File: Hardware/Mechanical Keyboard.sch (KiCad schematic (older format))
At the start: 24 parts, among them J1 USBMINI_B05, U1 ATMEGA32U4-AU, U2 IS31FL3731-SALS2, X1 ASX4

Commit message: Move diodes and resistors
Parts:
- C1, C2, C3, C4, C5, C6: symbol C -> Device:C
- J1: symbol USBMINI_B05 -> oupiin_usb:USBMINI_B05
- R1, R10, R11, R12, R13, R2, R3, R4, R5, R6, R7, R8, R9: symbol R -> Device:R
- S101: symbol DTSM-6 -> dtsjw:DTSM-6
- U1: symbol ATMEGA32U4-AU -> Mechanical-Keyboard-rescue:ATMEGA32U4-AU
- U2: symbol IS31FL3731-SALS2 -> ai03-locallib:IS31FL3731-SALS2
- X1: symbol ASX4 -> aker:ASX4
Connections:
- wire segments 143 -> 157

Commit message: refactor
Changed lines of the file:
@@
 Text Label 5800 5400 0    60   ~ 0
 swm_col3
-Text Label 5800 4700 0    60   ~ 0
+Text Label 5800 6600 0    60   ~ 0
 swm_col4
 Text Label 5800 5300 0    60   ~ 0
 swm_col5
-Text Label 5800 6600 0    60   ~ 0
+Text Label 5800 4700 0    60   ~ 0
 swm_col9
 Text Label 5800 6500 0    60   ~ 0
@@
 Wire Wire Line
 	13150 4000 12800 4000
+Text Label 13150 4100 2    60   ~ 0
+led_ca1
+Text Label 14250 4500 2    60   ~ 0
+led_ca2
+Text Label 13150 4300 2    60   ~ 0
+led_ca3
+Text Label 13150 3900 2    60   ~ 0
+led_ca4
+Text Label 13150 4000 2    60   ~ 0
+led_ca5
+Text Label 13150 4400 2    60   ~ 0
+led_ca6
+Text Label 13150 4500 2    60   ~ 0
+led_ca7
 Text Label 13150 3800 2    60   ~ 0
-led_ca1
-Text Label 13150 3900 2    60   ~ 0
-led_ca2
-Text Label 13150 4000 2    60   ~ 0
-led_ca3
-Text Label 13150 4100 2    60   ~ 0
-led_ca4
+led_ca8
 Text Label 13150 4200 2    60   ~ 0
-led_ca5
-Text Label 13150 4300 2    60   ~ 0
-led_ca6
-Text Label 13150 4400 2    60   ~ 0
-led_ca7
-Text Label 13150 4500 2    60   ~ 0
-led_ca8
-Text Label 14250 4500 2    60   ~ 0
 led_ca9
 Wire Wire Line

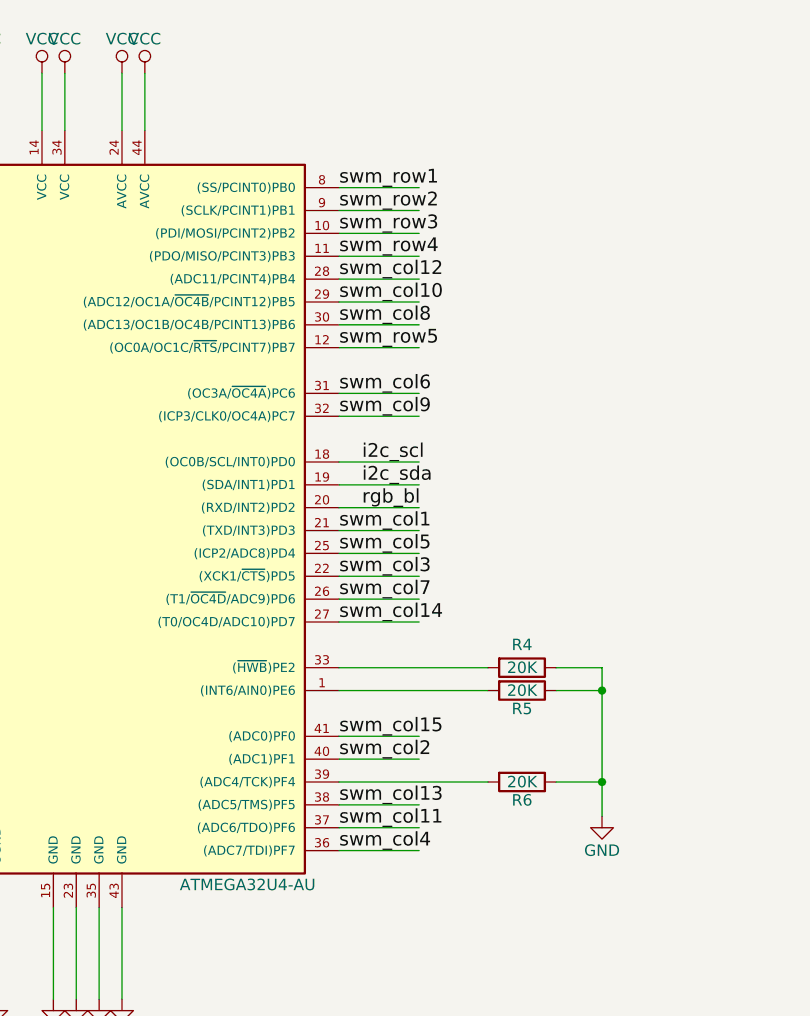
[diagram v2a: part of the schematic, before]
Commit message: Keyboard tracking was finished. Only GND circuit is left
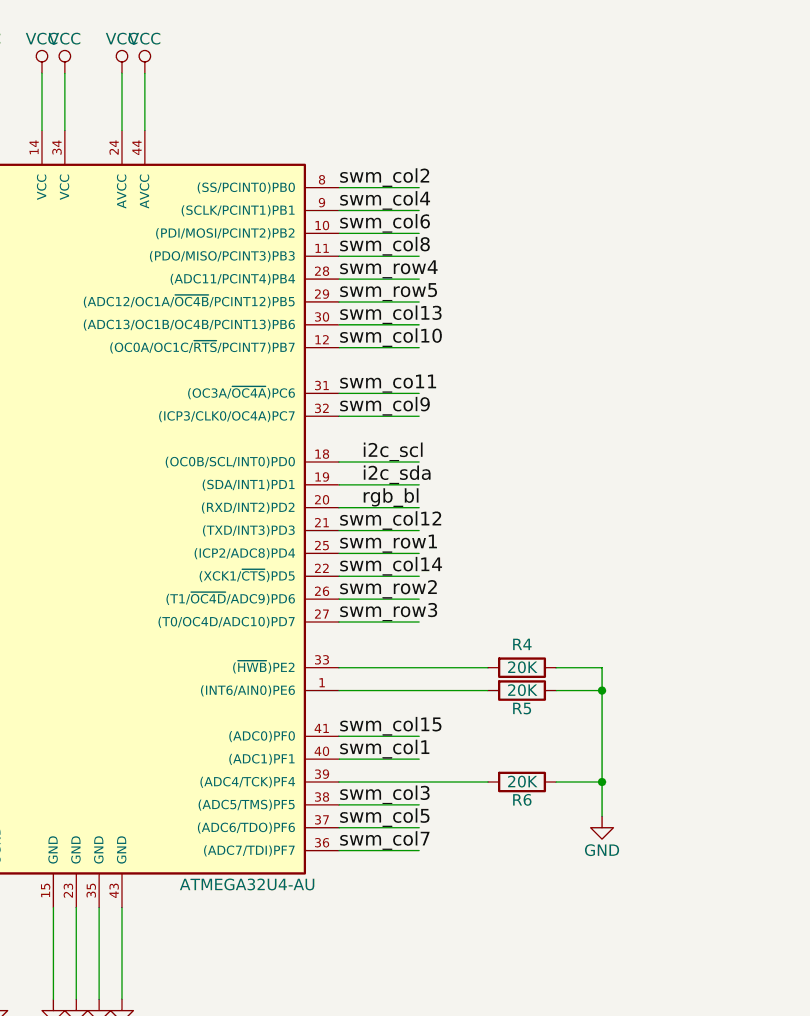
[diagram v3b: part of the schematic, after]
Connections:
- net labels added: swm_co11
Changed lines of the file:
@@
 swm_col14
 Text Label 5800 5200 0    60   ~ 0
+swm_col12
+Text Label 5800 6200 0    60   ~ 0
 swm_col1
-Text Label 5800 6200 0    60   ~ 0
-swm_col2
 Text Label 5800 5400 0    60   ~ 0
-swm_col3
+swm_col14
 Text Label 5800 6600 0    60   ~ 0
-swm_col4
+swm_col7
 Text Label 5800 5300 0    60   ~ 0
-swm_col5
+swm_row1
 Text Label 5800 4700 0    60   ~ 0
 swm_col9
 Text Label 5800 6500 0    60   ~ 0
-swm_col11
+swm_col5
 Text Label 5800 6400 0    60   ~ 0
-swm_col13
+swm_col3
 Text Label 5800 6100 0    60   ~ 0
 swm_col15
 Text Label 5800 5600 0    60   ~ 0
-swm_col14
+swm_row3
 Text Label 5800 5500 0    60   ~ 0
-swm_col7
+swm_row2
 Text Label 5800 4600 0    60   ~ 0
-swm_col6
+swm_co11
 Text Label 5800 4300 0    60   ~ 0
-swm_col8
+swm_col13
 Text Label 5800 4200 0    60   ~ 0
-swm_col10
+swm_row5
 Text Label 5800 4100 0    60   ~ 0
-swm_col12
+swm_row4
 Text Label 8500 3600 2    60   ~ 0
 swm_row1
@@
 swm_row5
 Text Label 5800 3700 0    60   ~ 0
-swm_row1
+swm_col2
 Text Label 5800 3800 0    60   ~ 0
-swm_row2
+swm_col4
 Text Label 5800 3900 0    60   ~ 0
-swm_row3
+swm_col6
 Text Label 5800 4000 0    60   ~ 0
-swm_row4
+swm_col8
 Text Label 5800 4400 0    60   ~ 0
-swm_row5
+swm_col10
 Text Label 11200 5900 2    60   ~ 0
 rgb_bl

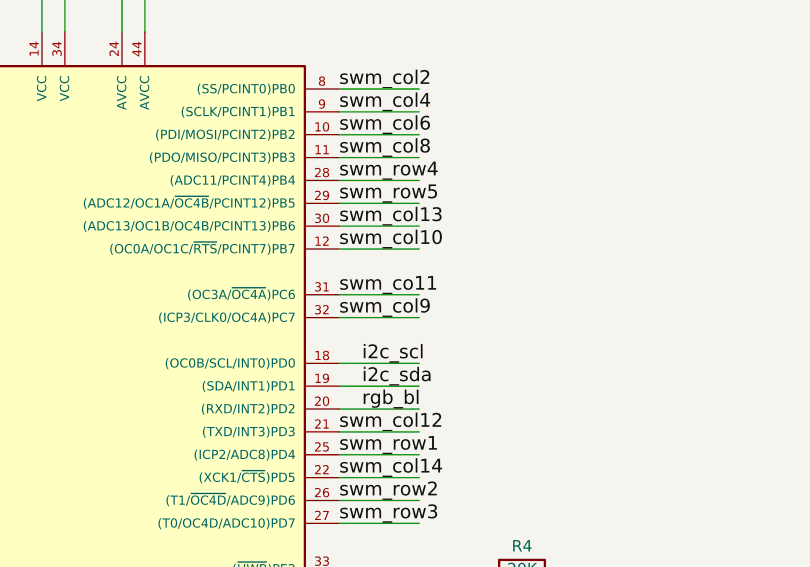
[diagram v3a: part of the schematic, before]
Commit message: Bugfix for swm_col9
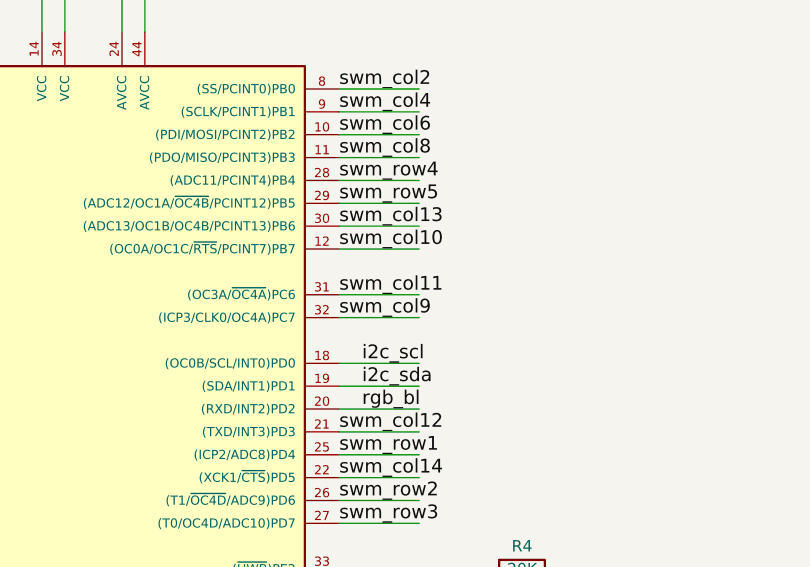
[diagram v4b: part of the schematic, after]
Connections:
- net labels removed: swm_co11
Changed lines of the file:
@@
 swm_row2
 Text Label 5800 4600 0    60   ~ 0
-swm_co11
+swm_col11
 Text Label 5800 4300 0    60   ~ 0
 swm_col13

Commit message: add driling holes
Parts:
- C1, C2, C3, C4, C5, C6: symbol Device:C -> Mechanical-Keyboard-rescue:C-Device
- R1, R10, R11, R12, R13, R2, R3, R4, R5, R6, R7, R8, R9: symbol Device:R -> Mechanical-Keyboard-rescue:R-Device
- U1: symbol Mechanical-Keyboard-rescue:ATMEGA32U4-AU -> Mechanical-Keyboard-rescue:ATMEGA32U4-AU-Mechanical-Keyboard-rescue
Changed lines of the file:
@@
 $EndSheet
 $Comp
-L power:GND #PWR01
+L Mechanical-Keyboard-rescue:GND-power #PWR01
 U 1 1 5C542506
 P 4750 7250
@@
 $EndComp
 $Comp
-L Mechanical-Keyboard-rescue:ATMEGA32U4-AU U1
+L Mechanical-Keyboard-rescue:ATMEGA32U4-AU-Mechanical-Keyboard-rescue U1
 U 1 1 5C4F1518
 P 4700 5250
@@
 $EndSheet
 $Comp
-L Device:R R7
+L Mechanical-Keyboard-rescue:R-Device R7
 U 1 1 5C4FF9D5
 P 11350 5900
@@
 $EndComp
 $Comp
-L power:VCC #PWR02
+L Mechanical-Keyboard-rescue:VCC-power #PWR02
 U 1 1 5C5072B7
 P 4500 3200
@@
 $EndComp
 $Comp
-L power:VCC #PWR03
+L Mechanical-Keyboard-rescue:VCC-power #PWR03
 U 1 1 5C50759B
 P 14650 3900
@@
 $EndComp
 $Comp
-L power:GND #PWR04
+L Mechanical-Keyboard-rescue:GND-power #PWR04
 U 1 1 5C507696
 P 14950 4250
@@
 $EndComp
 $Comp
-L power:VCC #PWR05
+L Mechanical-Keyboard-rescue:VCC-power #PWR05
 U 1 1 5C5087DF
 P 11100 6050
@@
 $EndComp
 $Comp
-L power:GND #PWR06
+L Mechanical-Keyboard-rescue:GND-power #PWR06
 U 1 1 5C508883
 P 11100 6200
@@
 $EndComp
 $Comp
-L power:GND #PWR07
+L Mechanical-Keyboard-rescue:GND-power #PWR07
 U 1 1 5C50B929
 P 11800 3550
@@
 $EndComp
 $Comp
-L power:GND #PWR08
+L Mechanical-Keyboard-rescue:GND-power #PWR08
 U 1 1 5C50C0CD
 P 6950 6450
@@
 $EndComp
 $Comp
-L Device:R R2
+L Mechanical-Keyboard-rescue:R-Device R2
 U 1 1 5C50D36F
 P 3150 5050
@@
 $EndComp
 $Comp
-L Device:R R3
+L Mechanical-Keyboard-rescue:R-Device R3
 U 1 1 5C50D676
 P 3150 5150
@@
 $EndComp
 $Comp
-L Device:C C1
+L Mechanical-Keyboard-rescue:C-Device C1
 U 1 1 5C50EABA
 P 3400 5550
@@
 $EndComp
 $Comp
-L power:GND #PWR09
+L Mechanical-Keyboard-rescue:GND-power #PWR09
 U 1 1 5C50EFE8
 P 3400 5800
@@
 $EndComp
 $Comp
-L power:VCC #PWR010
+L Mechanical-Keyboard-rescue:VCC-power #PWR010
 U 1 1 5C5804E3
 P 3400 4750
@@
 $EndComp
 $Comp
-L Device:C C2
+L Mechanical-Keyboard-rescue:C-Device C2
 U 1 1 5C580BB8
 P 1750 4650
@@
 $EndComp
 $Comp
-L Device:C C3
+L Mechanical-Keyboard-rescue:C-Device C3
 U 1 1 5C580CBE
 P 2350 4650
@@
 $EndComp
 $Comp
-L power:GND #PWR011
+L Mechanical-Keyboard-rescue:GND-power #PWR011
 U 1 1 5C58122B
 P 1750 4900
@@
 $EndComp
 $Comp
-L power:GND #PWR012
+L Mechanical-Keyboard-rescue:GND-power #PWR012
 U 1 1 5C58139C
 P 2350 4900
@@
 $EndComp
 $Comp
-L power:VCC #PWR013
+L Mechanical-Keyboard-rescue:VCC-power #PWR013
 U 1 1 5C58183B
 P 1850 1200
@@
 $EndComp
 $Comp
-L power:GND #PWR014
+L Mechanical-Keyboard-rescue:GND-power #PWR014
 U 1 1 5C581BA9
 P 1850 2000
@@
 $EndComp
 $Comp
-L Device:R R1
+L Mechanical-Keyboard-rescue:R-Device R1
 U 1 1 5C583CEE
 P 3450 3200
@@
 $EndComp
 $Comp
-L power:VCC #PWR015
+L Mechanical-Keyboard-rescue:VCC-power #PWR015
 U 1 1 5C584469
 P 3450 2900
@@
 $EndComp
 $Comp
-L Device:R R4
+L Mechanical-Keyboard-rescue:R-Device R4
 U 1 1 5C5F64E5
 P 6600 5800
@@
 $EndComp
 $Comp
-L power:GND #PWR016
+L Mechanical-Keyboard-rescue:GND-power #PWR016
 U 1 1 5C5FD875
 P 1500 4000
@@
 $EndComp
 $Comp
-L Device:C C4
+L Mechanical-Keyboard-rescue:C-Device C4
 U 1 1 5C608F79
 P 3400 6350
@@
 	5800 6200 6150 6200
 $Comp
-L power:GND #PWR017
+L Mechanical-Keyboard-rescue:GND-power #PWR017
 U 1 1 5C60BB3D
 P 3400 6550
@@
 	3400 6100 3550 6100
 $Comp
-L power:VCC #PWR018
+L Mechanical-Keyboard-rescue:VCC-power #PWR018
 U 1 1 5C60CED5
 P 4950 3200
@@
 $EndComp
 $Comp
-L power:VCC #PWR019
+L Mechanical-Keyboard-rescue:VCC-power #PWR019
 U 1 1 5C60CF9A
 P 4850 3200
@@
 $EndComp
 $Comp
-L power:VCC #PWR020
+L Mechanical-Keyboard-rescue:VCC-power #PWR020
 U 1 1 5C60D053
 P 4600 3200
@@
 $EndComp
 $Comp
-L power:VCC #PWR021
+L Mechanical-Keyboard-rescue:VCC-power #PWR021
 U 1 1 5C60D10C
 P 4250 3200
@@
 	4250 3200 4250 3450
 $Comp
-L power:GND #PWR022
+L Mechanical-Keyboard-rescue:GND-power #PWR022
 U 1 1 5C60DA59
 P 4850 7250
@@
 $EndComp
 $Comp
-L power:GND #PWR023
+L Mechanical-Keyboard-rescue:GND-power #PWR023
 U 1 1 5C60DB12
 P 4550 7250
@@
 $EndComp
 $Comp
-L power:GND #PWR024
+L Mechanical-Keyboard-rescue:GND-power #PWR024
 U 1 1 5C60DBCB
 P 4650 7250
@@
 $EndComp
 $Comp
-L power:GND #PWR025
+L Mechanical-Keyboard-rescue:GND-power #PWR025
 U 1 1 5C60DD41
 P 4300 7250
@@
 	6950 5800 6950 5900
 $Comp
-L Device:C C5
+L Mechanical-Keyboard-rescue:C-Device C5
 U 1 1 5C5EEF99
 P 11900 3300
@@
 Connection ~ 14950 4100
 $Comp
-L Device:R R8
+L Mechanical-Keyboard-rescue:R-Device R8
 U 1 1 5C5F33E7
 P 12450 3500
@@
 	11800 3500 11900 3500
 $Comp
-L Device:R R11
+L Mechanical-Keyboard-rescue:R-Device R11
 U 1 1 5C5F5FFC
 P 14250 4000
@@
 	13950 4000 14100 4000
 $Comp
-L Device:C C6
+L Mechanical-Keyboard-rescue:C-Device C6
 U 1 1 5C5F6F1C
 P 2500 1600
@@
 Connection ~ 1850 1850
 $Comp
-L Device:R R13
+L Mechanical-Keyboard-rescue:R-Device R13
 U 1 1 5C5FA03C
 P 14250 4300
@@
 Connection ~ 14650 4300
 $Comp
-L Device:R R12
+L Mechanical-Keyboard-rescue:R-Device R12
 U 1 1 5C5FAAE6
 P 14250 4200
@@
 Connection ~ 14650 4200
 $Comp
-L power:VCC #PWR026
+L Mechanical-Keyboard-rescue:VCC-power #PWR026
 U 1 1 5C600F03
 P 11400 3800
@@
 Connection ~ 12550 3600
 $Comp
-L Device:R R9
+L Mechanical-Keyboard-rescue:R-Device R9
 U 1 1 5C6014FC
 P 11950 3850
@@
 $EndComp
 $Comp
-L Device:R R10
+L Mechanical-Keyboard-rescue:R-Device R10
 U 1 1 5C6015EB
 P 11950 3950
@@
 usb_d+
 $Comp
-L Device:R R5
+L Mechanical-Keyboard-rescue:R-Device R5
 U 1 1 5C6895D0
 P 6600 5900
@@
 $EndComp
 $Comp
-L Device:R R6
+L Mechanical-Keyboard-rescue:R-Device R6
 U 1 1 5C68A00B
 P 6600 6300
@@
 Connection ~ 1750 4400
 $Comp
-L power:GND #PWR027
+L Mechanical-Keyboard-rescue:GND-power #PWR027
 U 1 1 5C5F19B1
 P 1950 4750
@@
 $EndComp
 $Comp
-L power:GND #PWR028
+L Mechanical-Keyboard-rescue:GND-power #PWR028
 U 1 1 5C5F1AC8
 P 2150 4750
